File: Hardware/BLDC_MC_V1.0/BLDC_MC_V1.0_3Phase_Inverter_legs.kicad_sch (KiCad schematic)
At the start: 30 parts, among them Q1 BSC027N10NS5ATMA1, Q2 BSC027N10NS5ATMA1, Q3 BSC027N10NS5ATMA1, Q4 BSC027N10NS5ATMA1, Q5 BSC027N10NS5ATMA1, Q6 BSC027N10NS5ATMA1

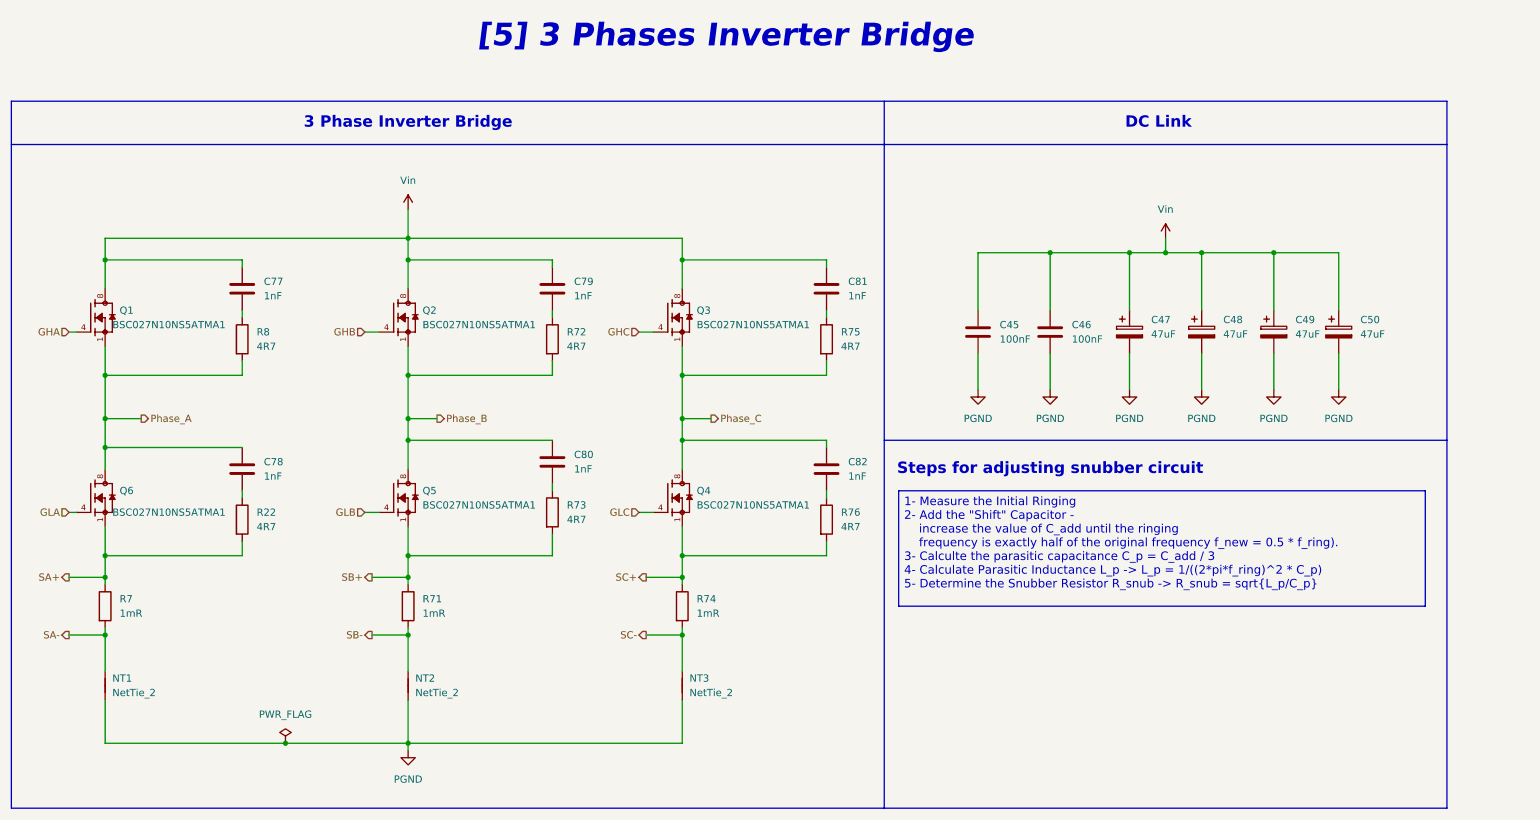
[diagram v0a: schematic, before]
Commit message: Routing Power plans and change the power connedtors
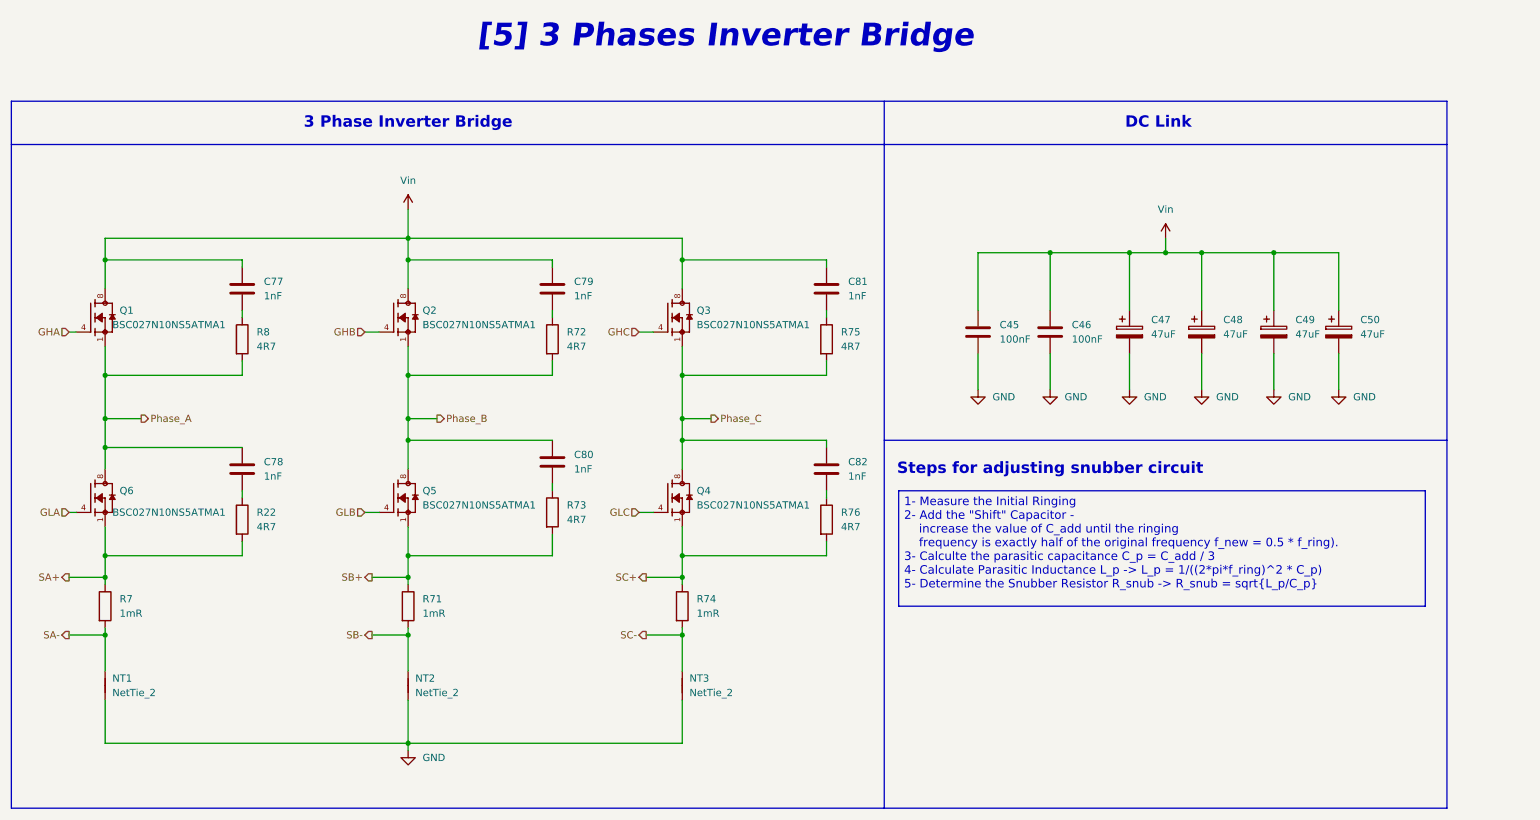
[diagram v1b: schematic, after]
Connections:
- net PGND renamed GND
